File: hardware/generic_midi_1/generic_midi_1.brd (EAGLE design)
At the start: 47.3 x 44.1 mm, 26 parts, among them IC1 MEGA168/328, IC2 RFM12

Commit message: test
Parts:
- removed JP10: PD6, pinhead:1X01
- removed JP11: PD4, pinhead:1X01
- removed JP12: PD3, pinhead:1X01
- removed JP13: PB7, pinhead:1X01
- removed JP14: PD0, pinhead:1X01
- removed JP9: PD5, pinhead:1X01
- JP6: value PB1 -> (none); device pinhead:1X01 -> pinhead:1X08
- JP7: value PB2 -> (none); device pinhead:1X01 -> pinhead:1X02
- JP8: value PD1 -> (none)
- moved JP8 33.2 mm to (36.8, 26.7)
- moved JP7 20.1 mm to (24.1, 3.81)
- moved JP6 15.6 mm to (38.1, 3.81)
- moved LED 6.74 mm to (27.9, 11.4)
- moved IC1 6.38 mm to (24.1, 19.1)
- moved IC2 6.38 mm to (25.4, 47.0)
- moved JP1 6.38 mm to (13.3, 45.1)
- moved JP2 6.38 mm to (10.2, 36.2)
- moved JP3 6.38 mm to (16.2, 31.4)
- moved JP5 6.38 mm to (44.1, 45.1)
- moved R4 6.38 mm to (42.9, 29.2)
- moved R5 6.38 mm to (21.0, 27.9)
- moved R7 6.38 mm to (6.99, 28.3)
- moved R8 6.38 mm to (6.99, 25.7)
- moved JP4 6.38 mm to (22.2, 10.2)
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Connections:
- removed net N$16: IC1.12, JP10.1
- removed net N$17: IC1.15, JP6.1
- removed net N$19: IC1.16, JP7.1
- removed net N$20: IC1.3, JP8.1
- removed net N$22: IC1.6, JP11.1
- removed net N$23: IC1.5, JP12.1
- removed net N$25: IC1.10, JP13.1
- removed net N$26: IC1.2, JP14.1
- new net IO0: IC1.3, JP6.1
- new net IO1: IC1.2, JP6.2
- new net IO2: IC1.5, JP6.3
- new net IO3: IC1.6, JP6.4
- new net IO4: IC1.11, JP6.5
- new net IO5: IC1.12, JP6.6
- new net IO6: IC1.15, JP6.7
- new net IO7: IC1.16, JP6.8
- net N$14: now also IC1.10, JP7.1, JP7.2; no longer IC1.11, JP9.1
- net N$24: now also JP8.1
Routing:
- net IO1: track 0.00 -> 33.6 mm
- net IO7: track 0.00 -> 30.4 mm
- net IO3: track 0.00 -> 29.3 mm
- net IO2: track 0.00 -> 25.7 mm
- net IO0: track 0.00 -> 23.5 mm
- net IO6: track 0.00 -> 21.4 mm
- net IO5: track 0.00 -> 14.1 mm
- net IO4: track 0.00 -> 14.1 mm
- net N$24: track 17.1 -> 26.6 mm
- net N$23: track 5.78 -> 0.00 mm
- net N$22: track 5.78 -> 0.00 mm
- net N$26: track 5.71 -> 0.00 mm
- net N$20: track 5.71 -> 0.00 mm
- net N$25: track 5.21 -> 0.00 mm
- net N$16: track 4.93 -> 0.00 mm
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- removed copper zone on layer 1, net GND
- removed copper zone on layer 16, net GND
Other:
- board size 47.3 x 44.1 mm -> 49.8 x 51.8 mm

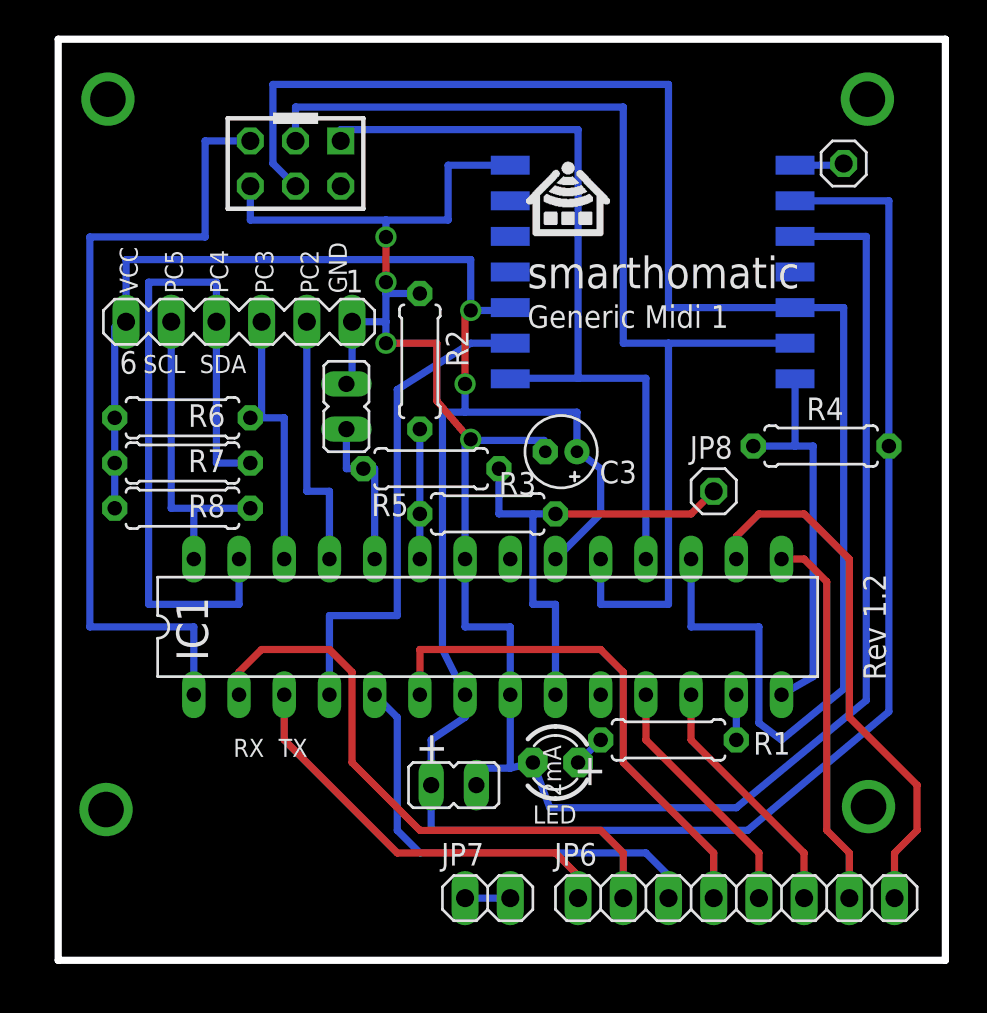
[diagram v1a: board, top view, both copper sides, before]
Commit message: fix transistor
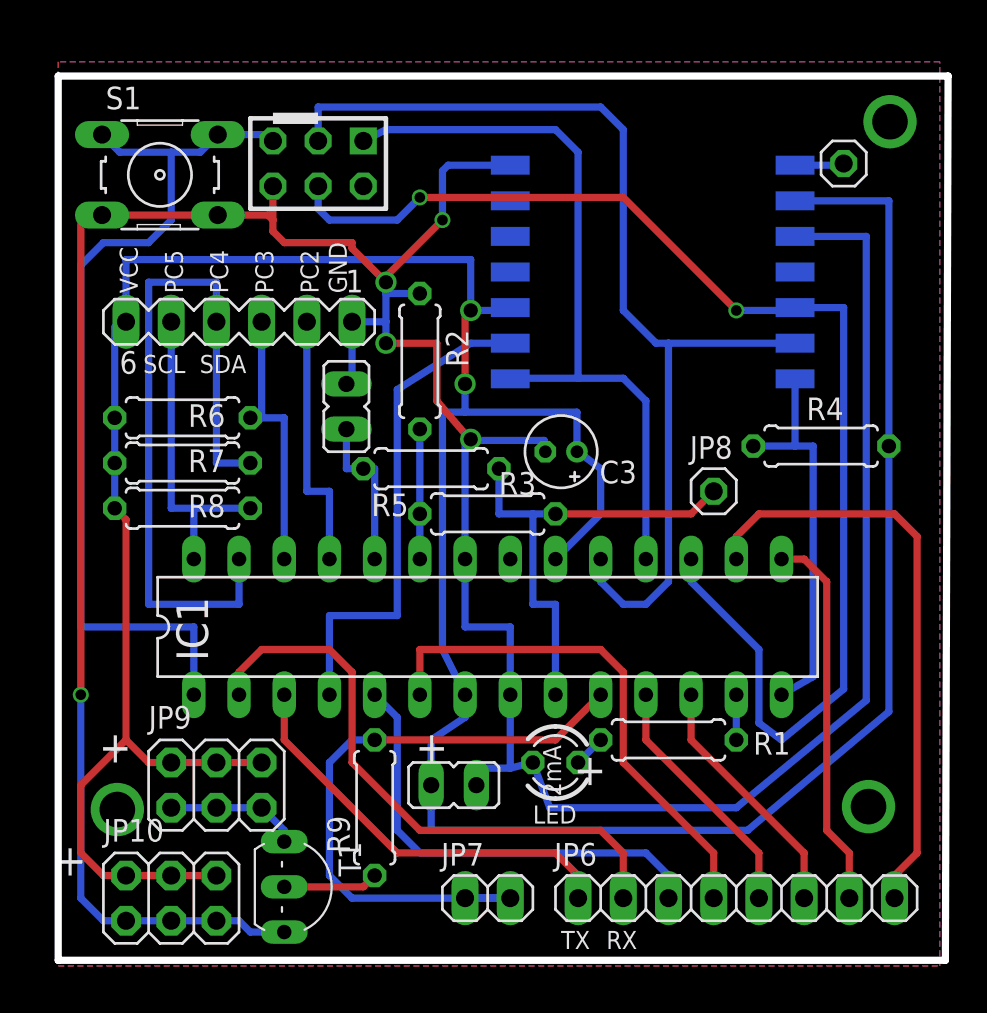
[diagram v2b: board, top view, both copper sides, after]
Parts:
- added JP10, JP9: (no value), pinhead:2X03
- added R9: 560, rcl:0207/7
- added S1: (no value), switch-omron:B3F-10XX
- added T1: (no value), transistor:TO92-CBE
- moved JP1 1.27 mm to (14.6, 45.1)
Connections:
- new net N$16: JP9.1, JP9.3, JP9.5, T1.C
- new net N$17: R9.1, T1.B
- net GND: now also JP10.1, JP10.3, JP10.5, S1.3, S1.4, T1.E
- net N$14: now also R9.2
- net N$8: now also S1.1, S1.2
- net VCC: now also JP10.2, JP10.4, JP10.6, JP9.2, JP9.4, JP9.6
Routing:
- net GND: track 126.5 -> 186.6 mm, vias 4 -> 5
- net VCC: track 149.4 -> 189.0 mm
- net N$14: track 2.54 -> 36.4 mm
- net N$3: track 91.4 -> 72.6 mm, vias 0 -> 2
- net N$16: track 0.00 -> 7.51 mm
- net N$17: track 0.00 -> 5.34 mm
- net N$8: track 46.0 -> 51.0 mm
- net N$5: track 64.3 -> 59.7 mm
- net N$4: track 45.8 -> 42.5 mm
- net IO7: track 30.4 -> 33.3 mm
- added copper zone on layer 1, net GND
- added copper zone on layer 16, net GND
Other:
- board size 49.8 x 51.8 mm -> 50 x 49.7 mm
- board text removed: "D:/Eigene Dateien/smarthomatic/logo/logo_black 150x133.bmp"
- board text removed: "Generic Midi 1"
- board text removed: "Rev 1.2"
- board text removed: "smarthomatic"
